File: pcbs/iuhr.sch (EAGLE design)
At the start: 75 parts, among them IC1 TPS77033, Q1 20.000MHz

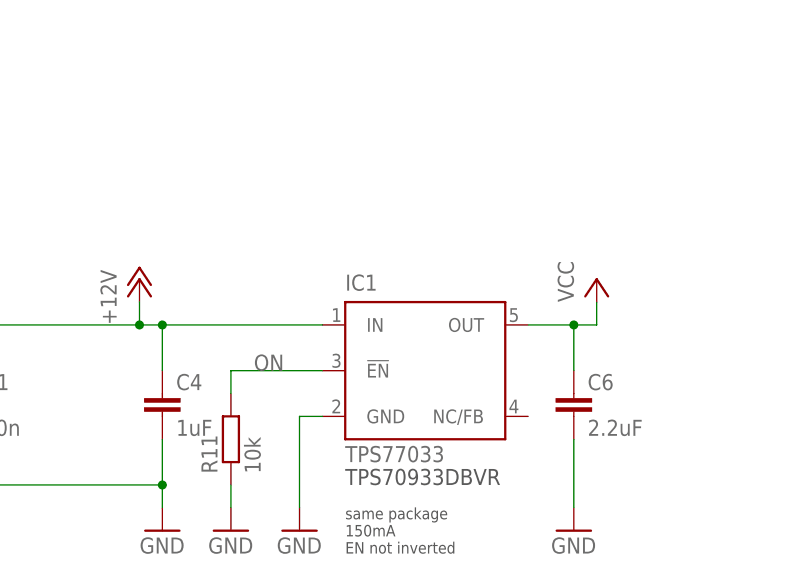
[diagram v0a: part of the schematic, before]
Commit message: Further improve silkscreen.
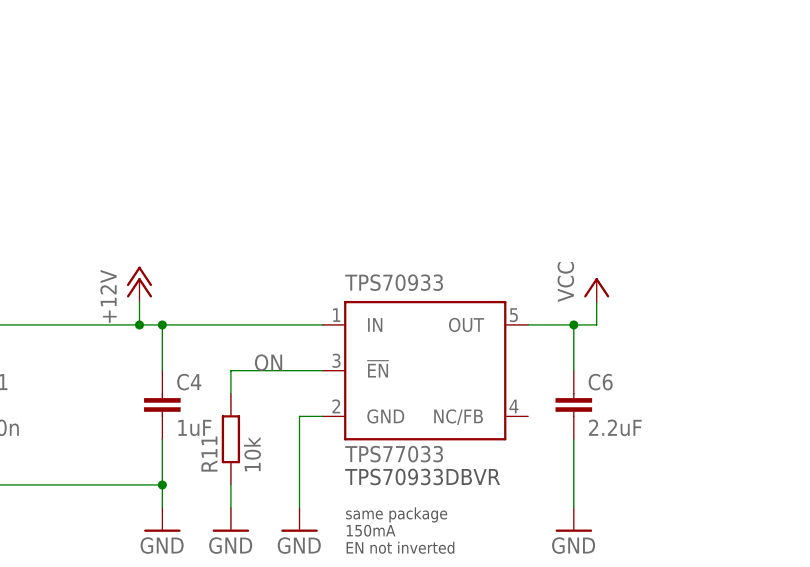
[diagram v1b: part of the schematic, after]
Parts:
- renumbered IC1 to TPS70933
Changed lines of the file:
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@@
 <part name="GND10" library="supply1" deviceset="GND" device=""/>
 <part name="R10" library="resistor" deviceset="R-EU_" device="R0603" value="0"/>
-<part name="IC1" library="texas" deviceset="TPS770*" device="" technology="33"/>
+<part name="TPS70933" library="texas" deviceset="TPS770*" device="" technology="33"/>
 <part name="P+16" library="supply1" deviceset="+12V" device=""/>
 <part name="P+17" library="supply1" deviceset="VCC" device=""/>
@@
 <instance part="GND10" gate="1" x="27.94" y="-76.2"/>
 <instance part="R10" gate="G$1" x="27.94" y="-66.04" rot="R90"/>
-<instance part="IC1" gate="G$1" x="119.38" y="43.18"/>
+<instance part="TPS70933" gate="G$1" x="119.38" y="43.18"/>
 <instance part="P+16" gate="1" x="88.9" y="53.34"/>
 <instance part="P+17" gate="VCC" x="139.7" y="53.34"/>
@@
 <pinref part="GND11" gate="1" pin="GND"/>
 <wire x1="106.68" y1="27.94" x2="106.68" y2="38.1" width="0.1524" layer="91"/>
-<pinref part="IC1" gate="G$1" pin="GND"/>
+<pinref part="TPS70933" gate="G$1" pin="GND"/>
 <wire x1="106.68" y1="38.1" x2="109.22" y2="38.1" width="0.1524" layer="91"/>
 </segment>
@@
 </segment>
 <segment>
-<pinref part="IC1" gate="G$1" pin="OUT"/>
+<pinref part="TPS70933" gate="G$1" pin="OUT"/>
 <pinref part="P+17" gate="VCC" pin="VCC"/>
 <wire x1="132.08" y1="48.26" x2="137.16" y2="48.26" width="0.1524" layer="91"/>
@@
 <pinref part="P+16" gate="1" pin="+12V"/>
 <wire x1="88.9" y1="50.8" x2="88.9" y2="48.26" width="0.1524" layer="91"/>
-<pinref part="IC1" gate="G$1" pin="IN"/>
+<pinref part="TPS70933" gate="G$1" pin="IN"/>
 <wire x1="88.9" y1="48.26" x2="91.44" y2="48.26" width="0.1524" layer="91"/>
 <junction x="91.44" y="48.26"/>
@@
 <net name="ON" class="0">
 <segment>
-<pinref part="IC1" gate="G$1" pin="!EN"/>
+<pinref part="TPS70933" gate="G$1" pin="!EN"/>
 <wire x1="109.22" y1="43.18" x2="99.06" y2="43.18" width="0.1524" layer="91"/>
 <wire x1="99.06" y1="43.18" x2="99.06" y2="40.64" width="0.1524" layer="91"/>

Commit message: VCC: 3.3V -> 5V; add cap for adg3123
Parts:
- added C7: 100nF, resistor:C-EUC0603
- TPS70933: value TPS77033 -> TPS77050; device texas:TPS77033 -> texas:TPS77050
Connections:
- net +12V: now also C7.1
- net GND: now also C7.2
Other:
- note added: "TPS70950DBVR"
- note removed: "TPS70933DBVR"
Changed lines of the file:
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@@
 <part name="GND10" library="supply1" deviceset="GND" device=""/>
 <part name="R10" library="resistor" deviceset="R-EU_" device="R0603" value="0"/>
-<part name="TPS70933" library="texas" deviceset="TPS770*" device="" technology="33"/>
+<part name="TPS70933" library="texas" deviceset="TPS770*" device="" technology="50" value="TPS77050"/>
 <part name="P+16" library="supply1" deviceset="+12V" device=""/>
 <part name="P+17" library="supply1" deviceset="VCC" device=""/>
@@
 <part name="PD5" library="testpad" deviceset="TP" device="TP15SQ"/>
 <part name="PB7" library="testpad" deviceset="TP" device="TP15SQ"/>
+<part name="C7" library="resistor" deviceset="C-EU" device="C0603" value="100nF"/>
+<part name="GND17" library="supply1" deviceset="GND" device=""/>
+<part name="P+21" library="supply1" deviceset="+12V" device=""/>
 </parts>
 <sheets>
@@
 <text x="132.08" y="157.48" size="1.778" layer="97">atmega88a-pa</text>
 <text x="20.32" y="-106.68" size="1.778" layer="97">Max Current: 40mA</text>
-<text x="111.76" y="30.48" size="1.778" layer="97">TPS70933DBVR</text>
+<text x="111.76" y="30.48" size="1.778" layer="97">TPS70950DBVR</text>
 <text x="111.76" y="22.86" size="1.27" layer="97">same package
 150mA
@@
 <instance part="PD5" gate="G$1" x="182.88" y="116.84" rot="R270"/>
 <instance part="PB7" gate="G$1" x="101.6" y="132.08" rot="MR270"/>
+<instance part="C7" gate="G$1" x="177.8" y="-30.48"/>
+<instance part="GND17" gate="1" x="177.8" y="-40.64"/>
+<instance part="P+21" gate="1" x="177.8" y="-22.86"/>
 </instances>
 <busses>
@@
 <pinref part="GND16" gate="1" pin="GND"/>
 <wire x1="68.58" y1="-114.3" x2="68.58" y2="-111.76" width="0.1524" layer="91"/>
+</segment>
+<segment>
+<pinref part="C7" gate="G$1" pin="2"/>
+<pinref part="GND17" gate="1" pin="GND"/>
+<wire x1="177.8" y1="-38.1" x2="177.8" y2="-35.56" width="0.1524" layer="91"/>
 </segment>
 </net>
@@
 <junction x="68.58" y="48.26"/>
 </segment>
-</net>
+<segment>
+<pinref part="C7" gate="G$1" pin="1"/>
+<wire x1="177.8" y1="-25.4" x2="177.8" y2="-27.94" width="0.1524" layer="91"/>
+<pinref part="P+21" gate="1" pin="+12V"/>
+</segment>
+</net>

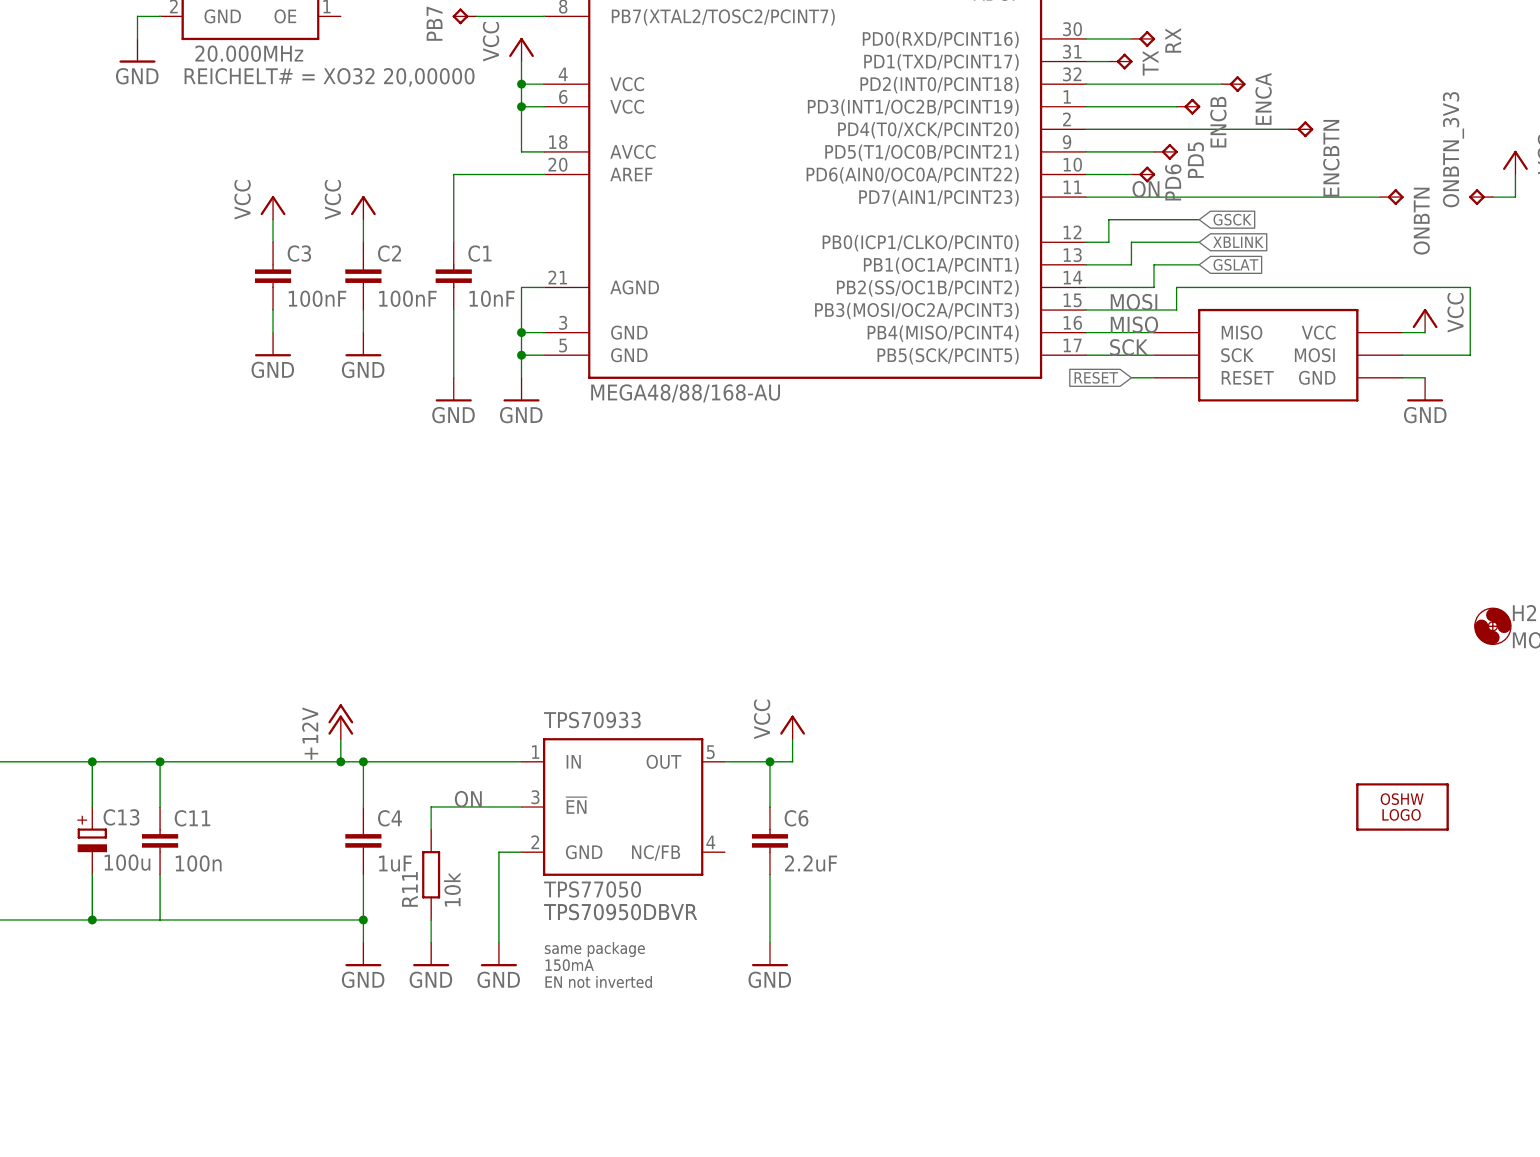
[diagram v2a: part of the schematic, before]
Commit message: Power On: add cap and series resistor for button.
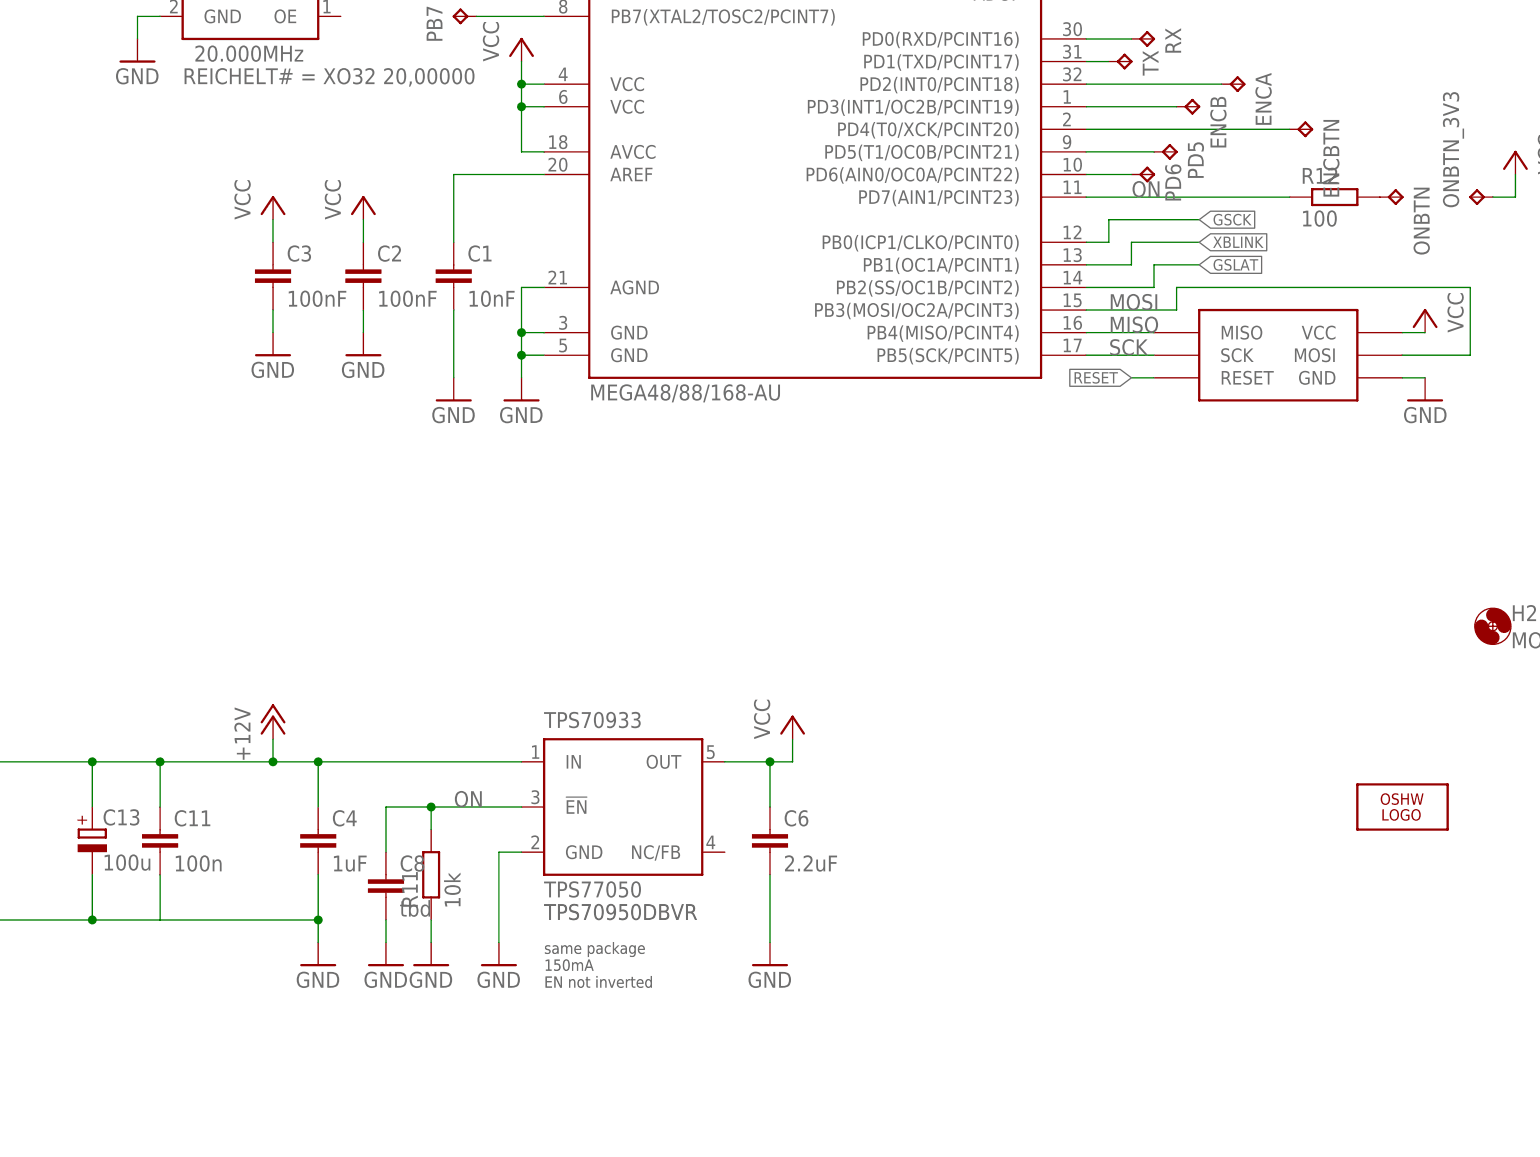
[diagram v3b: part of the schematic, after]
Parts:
- added C8: tbd, resistor:C-EUC0603
- added R12: 100, resistor:R-EU_R0603
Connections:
- new net N$59: ONBTN.TP, R12.2
- net GND: now also C8.2
- net ON: now also C8.1, R12.1; no longer ONBTN.TP
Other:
- moved on the sheet: C4
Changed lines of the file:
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@@
 <part name="GND17" library="supply1" deviceset="GND" device=""/>
 <part name="P+21" library="supply1" deviceset="+12V" device=""/>
+<part name="C8" library="resistor" deviceset="C-EU" device="C0603" value="tbd"/>
+<part name="GND18" library="supply1" deviceset="GND" device=""/>
+<part name="R12" library="resistor" deviceset="R-EU_" device="R0603" value="100"/>
 </parts>
 <sheets>
@@
 <instance part="R10" gate="G$1" x="27.94" y="-66.04" rot="R90"/>
 <instance part="TPS70933" gate="G$1" x="119.38" y="43.18"/>
-<instance part="P+16" gate="1" x="88.9" y="53.34"/>
+<instance part="P+16" gate="1" x="81.28" y="53.34"/>
 <instance part="P+17" gate="VCC" x="139.7" y="53.34"/>
 <instance part="GND11" gate="1" x="106.68" y="25.4"/>
 <instance part="R11" gate="G$1" x="99.06" y="35.56" rot="R90"/>
 <instance part="GND12" gate="1" x="99.06" y="25.4"/>
-<instance part="C4" gate="G$1" x="91.44" y="40.64"/>
-<instance part="GND13" gate="1" x="91.44" y="25.4"/>
+<instance part="C4" gate="G$1" x="86.36" y="40.64"/>
+<instance part="GND13" gate="1" x="86.36" y="25.4"/>
 <instance part="C6" gate="G$1" x="137.16" y="40.64"/>
 <instance part="GND14" gate="1" x="137.16" y="25.4"/>
@@
 <instance part="GND17" gate="1" x="177.8" y="-40.64"/>
 <instance part="P+21" gate="1" x="177.8" y="-22.86"/>
+<instance part="C8" gate="G$1" x="93.98" y="35.56"/>
+<instance part="GND18" gate="1" x="93.98" y="25.4"/>
+<instance part="R12" gate="G$1" x="200.66" y="111.76"/>
 </instances>
 <busses>
@@
 <segment>
 <pinref part="C4" gate="G$1" pin="2"/>
-<wire x1="91.44" y1="35.56" x2="91.44" y2="30.48" width="0.1524" layer="91"/>
+<wire x1="86.36" y1="35.56" x2="86.36" y2="30.48" width="0.1524" layer="91"/>
 <pinref part="GND13" gate="1" pin="GND"/>
-<wire x1="91.44" y1="30.48" x2="91.44" y2="27.94" width="0.1524" layer="91"/>
-<wire x1="91.44" y1="30.48" x2="68.58" y2="30.48" width="0.1524" layer="91"/>
+<wire x1="86.36" y1="30.48" x2="86.36" y2="27.94" width="0.1524" layer="91"/>
+<wire x1="86.36" y1="30.48" x2="68.58" y2="30.48" width="0.1524" layer="91"/>
 <pinref part="GND_IN" gate="G$1" pin="TP"/>
-<junction x="91.44" y="30.48"/>
+<junction x="86.36" y="30.48"/>
 <pinref part="C11" gate="G$1" pin="2"/>
 <wire x1="68.58" y1="30.48" x2="60.96" y2="30.48" width="0.1524" layer="91"/>
@@
 <pinref part="GND17" gate="1" pin="GND"/>
 <wire x1="177.8" y1="-38.1" x2="177.8" y2="-35.56" width="0.1524" layer="91"/>
+</segment>
+<segment>
+<pinref part="C8" gate="G$1" pin="2"/>
+<pinref part="GND18" gate="1" pin="GND"/>
+<wire x1="93.98" y1="27.94" x2="93.98" y2="30.48" width="0.1524" layer="91"/>
 </segment>
 </net>
@@
 <segment>
 <pinref part="P+16" gate="1" pin="+12V"/>
-<wire x1="88.9" y1="50.8" x2="88.9" y2="48.26" width="0.1524" layer="91"/>
+<wire x1="81.28" y1="50.8" x2="81.28" y2="48.26" width="0.1524" layer="91"/>
 <pinref part="TPS70933" gate="G$1" pin="IN"/>
-<wire x1="88.9" y1="48.26" x2="91.44" y2="48.26" width="0.1524" layer="91"/>
-<junction x="91.44" y="48.26"/>
-<wire x1="91.44" y1="48.26" x2="109.22" y2="48.26" width="0.1524" layer="91"/>
+<wire x1="81.28" y1="48.26" x2="86.36" y2="48.26" width="0.1524" layer="91"/>
+<junction x="86.36" y="48.26"/>
+<wire x1="86.36" y1="48.26" x2="109.22" y2="48.26" width="0.1524" layer="91"/>
 <pinref part="C4" gate="G$1" pin="1"/>
-<wire x1="91.44" y1="48.26" x2="91.44" y2="43.18" width="0.1524" layer="91"/>
+<wire x1="86.36" y1="48.26" x2="86.36" y2="43.18" width="0.1524" layer="91"/>
 <pinref part="12V_IN" gate="G$1" pin="TP"/>
 <wire x1="40.64" y1="48.26" x2="60.96" y2="48.26" width="0.1524" layer="91"/>
-<junction x="88.9" y="48.26"/>
+<junction x="81.28" y="48.26"/>
 <pinref part="C13" gate="G$1" pin="+"/>
 <wire x1="60.96" y1="48.26" x2="68.58" y2="48.26" width="0.1524" layer="91"/>
-<wire x1="68.58" y1="48.26" x2="88.9" y2="48.26" width="0.1524" layer="91"/>
+<wire x1="68.58" y1="48.26" x2="81.28" y2="48.26" width="0.1524" layer="91"/>
 <wire x1="60.96" y1="43.18" x2="60.96" y2="48.26" width="0.1524" layer="91"/>
 <pinref part="C11" gate="G$1" pin="1"/>
@@
 <pinref part="R11" gate="G$1" pin="2"/>
 <label x="101.6" y="43.18" size="1.778" layer="95"/>
+<pinref part="C8" gate="G$1" pin="1"/>
+<wire x1="93.98" y1="38.1" x2="93.98" y2="43.18" width="0.1524" layer="91"/>
+<wire x1="93.98" y1="43.18" x2="99.06" y2="43.18" width="0.1524" layer="91"/>
+<junction x="99.06" y="43.18"/>
 </segment>
 <segment>
 <pinref part="ATMEGA88PA" gate="1" pin="PD7(AIN1/PCINT23)"/>
-<wire x1="172.72" y1="111.76" x2="205.74" y2="111.76" width="0.1524" layer="91"/>
+<wire x1="172.72" y1="111.76" x2="195.58" y2="111.76" width="0.1524" layer="91"/>
 <label x="177.8" y="111.76" size="1.778" layer="95"/>
-<pinref part="ONBTN" gate="G$1" pin="TP"/>
+<pinref part="R12" gate="G$1" pin="1"/>
 </segment>
 </net>
@@
 </segment>
 </net>
+<net name="N$59" class="0">
+<segment>
+<pinref part="ONBTN" gate="G$1" pin="TP"/>
+<pinref part="R12" gate="G$1" pin="2"/>
+</segment>
+</net>
